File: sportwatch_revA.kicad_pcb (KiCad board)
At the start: 2 copper layers, 228 parts, among them J1 ZC-A1D43W-046, J1301 TC2030-CTX-NL_TARGET, U101 AP510BFA-CBR, U102 SN74AXC8T245, U103 TXB0101DRLR, U104 SN74AXC1T45, U105 SN74AXC1T45, U106 PCA9306DCU, U11 TPS22918DBVT, U12 MAX86141ENP+T, U13 MAX86141ENP+T, U201 nPM1300-QEXX, U202 TPS63900, U4 BMP585, U401 TPS631000DRLR, U402 TS5A12301E, U403 TS5A12301E, U404 TS5A12301E, U405 TS5A12301E, U406 TS5A12301E, U407 TS5A12301E, U5 OPT4001DTSR, U6 MAX30208CLB+T, U7 DRV2625YFFR, U702 LSM6DSV16XTR, U703 BMM350, U8 MAX-F10S-00B, U9 NRF7002-QFAA-R7, U901 EMMC64G-TB9F-06011, Y1 40MHz_CL8pF_ESR100R_1612, Y101 32.768kHz / low-CL TBD, Y102 48MHz / CL=8-11pF / ESR<=60R

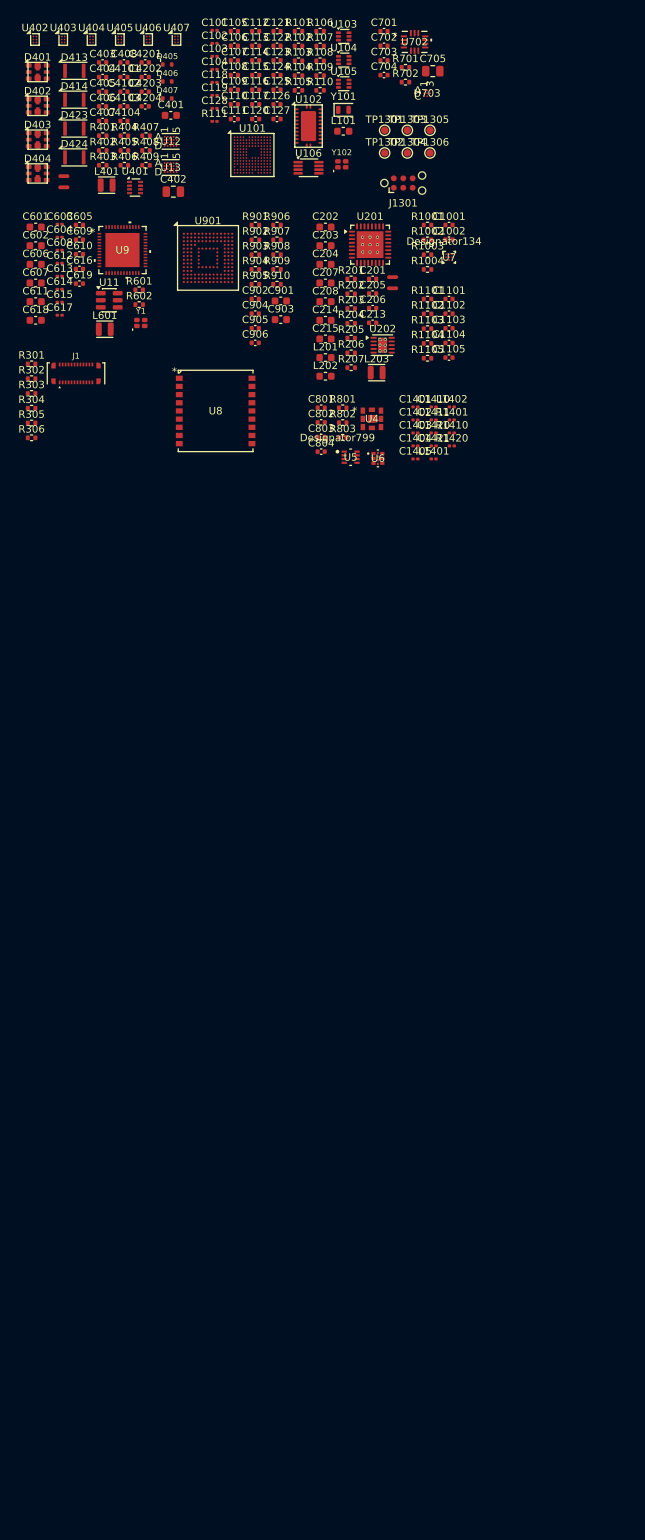
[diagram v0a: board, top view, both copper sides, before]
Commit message: feat(pcb): establish 8-layer HDI foundation, 46mm outline, and critical cluster feasibility
- Configure 8-layer HDI Type III (2+4+2) 0.808mm stackup in sportwatch_revA.kicad_pcb
- Configure design rules in sportwatch_revA.kicad_pro and sportwatch_revA.kicad_dru (0.20/0.10mm microvias, 0.075mm trace/space)
- Define provisional 46.0mm circular board outline on Edge.Cuts
- Add IPC courtyards to NT201, NT202, NT401, NT402, U5, and U7
- Provisionally place and validate 7 critical clusters (61 placed parts) with 0 courtyard overlaps and >=2.2mm edge margin
- Demonstrate representative Apollo510B and eMMC escape fanout with VIPPO and stacked microvias
- Author docs/project/pcb_foundation_revA.md and docs/project/critical_cluster_feasibility.md
- Update docs/project/AGENT_HANDOFF.md with PASS verdict
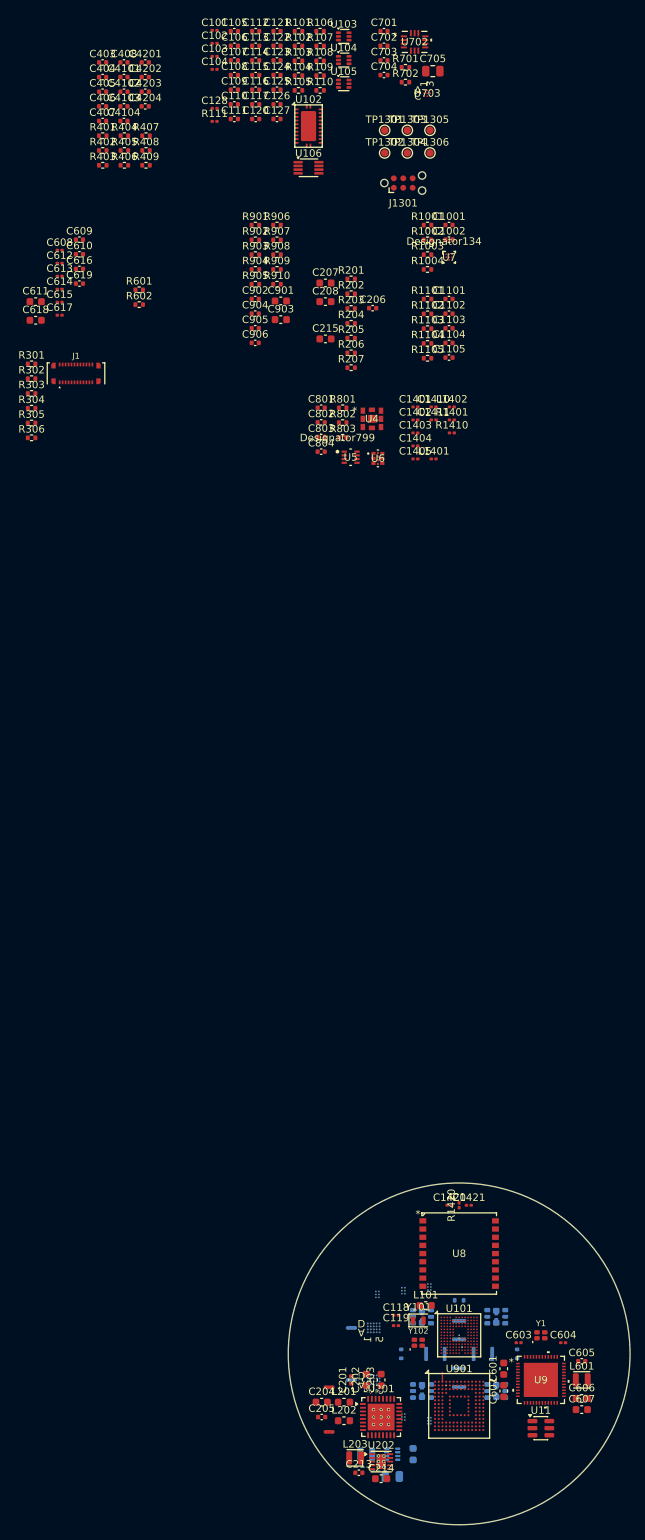
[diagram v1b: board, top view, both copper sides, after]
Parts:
- C401, C402, D401, D402, D403, D404, D405, D406, D407, D413, D414, D423, D424, L401, NT401, NT402, U12, U13, U401, U402, U403, U404, U405, U406, U407: moved to B.Cu
- moved U407 189.0 mm to (96.0, 109.0)
- moved U406 188.6 mm to (92.5, 108.5)
- moved U405 188.1 mm to (89.0, 108.0)
- moved C401 183.1 mm to (93.8, 113.5), turned to 90 degrees
- moved D414 179.6 mm to (100.0, 103.2), turned to 90 degrees
- moved D413 177.2 mm to (100.0, 96.8), turned to 90 degrees
- moved D405 176.4 mm to (92.2, 100.0), turned to 90 degrees
- moved D403 176.2 mm to (95.0, 105.0)
- moved C402 175.4 mm to (91.0, 116.5)
- moved D407 175.4 mm to (107.8, 100.0), turned to 90 degrees
- moved D401 175.3 mm to (95.0, 95.0)
- moved D404 175.1 mm to (105.0, 105.0)
- moved U402 175.1 mm to (89.0, 92.0)
- moved U403 174.5 mm to (92.5, 91.5)
- moved L401 174.3 mm to (87.5, 113.5)
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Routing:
- net /EMMC_DAT4: track 0.00 -> 2.60 mm, vias 0 -> 2
- net /EMMC_DAT5: track 0.00 -> 1.75 mm, vias 0 -> 2
- net /EMMC_DAT7: track 0.00 -> 1.40 mm, vias 0 -> 2
- net /EMMC_DAT0: track 0.00 -> 1.25 mm
- net GND: track 0.00 -> 0.10 mm, vias 0 -> 1
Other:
- board outline added: 46 x 46 mm
- copper layers 2 -> 8

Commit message: fix(pcb): complete all 18 foundation corrections from Codex review
- Eliminate 8 cross-side shorts and 18 solder mask bridges
- Relocate TPS631000 cluster to F.Cu per TI reference layout
- Relocate U405/U406/U407 on B.Cu clear of U201/U202 thermal keepouts
- Redesign PPG optical island with U12/U13 pin-optimized coordinates (up to 87.5% distance reduction)
- Rotate nRF7002 (180 deg) and MAX-F10S (90 deg) towards antenna feeds
- Place Apollo RTC/BLE crystals with <2.4mm pad lines and 0 overlaps
- Place nPM1300/TPS63900 buck passives with 0 collisions and zero edge errors
- Implement continuous ground reference planes on In1.Cu and In6.Cu
- Configure B.Cu thermal keepouts under U201/U202 and solid plane connectivity
- Strip dangling trial tracks and microvias
- Fix malformed courtyard geometry on U4 (BMP585)
- Reconcile net count (389 named nets 1:1) and hierarchical interfaces (0 mismatches)
- Verify native KiCad DRC (0 errors) and schematic parity (0 issues)
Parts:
- C401, C402, L401, U401: moved to F.Cu
- moved C215 155.4 mm to (89.5, 118.6)
- moved C208 151.1 mm to (81.0, 109.5)
- moved C207 150.6 mm to (81.0, 106.5)
- moved U12 15.4 mm to (100.0, 106.8)
- moved C205 12.1 mm to (93.6, 107.5), turned to 90 degrees
- moved L601 10.7 mm to (105.8, 103.8), turned to 90 degrees
- moved C119 10.5 mm to (101.6, 93.3)
- moved L401 8.99 mm to (95.5, 117.6)
- moved C402 7.67 mm to (98.4, 114.5), turned to 90 degrees
- moved U405 6.50 mm to (95.0, 110.5)
- moved U406 5.85 mm to (98.0, 110.5)
- moved U407 5.22 mm to (101.0, 110.5)
- moved C118 5.12 mm to (96.4, 93.3)
- moved Y101 5.01 mm to (99.0, 93.3)
- moved U401 4.61 mm to (95.5, 114.5)
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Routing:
- net /EMMC_DAT4: track 2.60 -> 0.00 mm, vias 2 -> 0
- net /EMMC_DAT5: track 1.75 -> 0.00 mm, vias 2 -> 0
- net /EMMC_DAT7: track 1.40 -> 0.00 mm, vias 2 -> 0
- net /EMMC_DAT0: track 1.25 -> 0.00 mm
- net GND: track 0.10 -> 0.00 mm, vias 1 -> 0
- added copper zone on In1.Cu, net GND
- added copper zone on In6.Cu, net GND

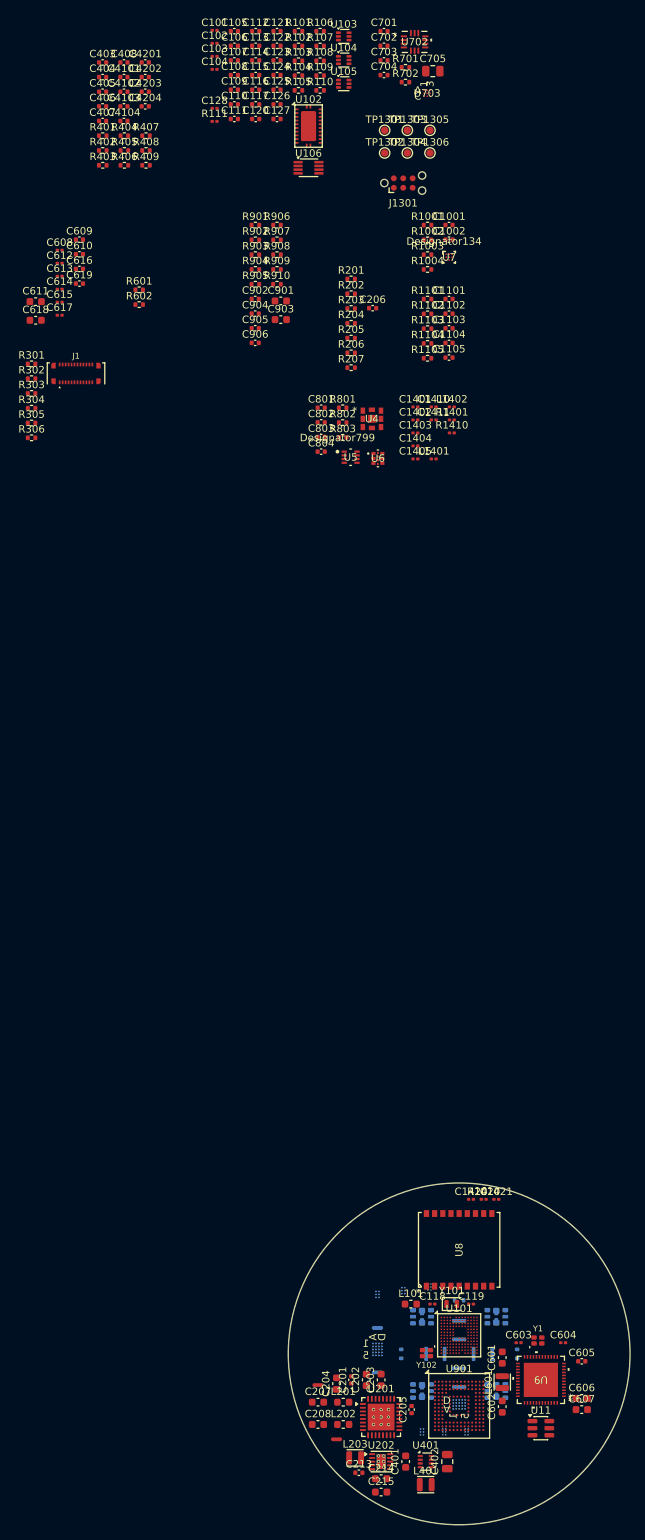
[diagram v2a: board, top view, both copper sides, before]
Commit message: fix(pcb): complete foundation correction round 2 with verified DRC 0 errors
- Phase 0 & Checkpoint A: Reconcile repository state to HEAD ecd5eda, preserving Section 7 reviewer notes; verify 0 shorts, 0 clearance errors
- Phase 1: Verify cross-side isolation for U201/U202 thermal fields clear of B.Cu; restore B.Cu keepout rule areas (Zone 0 & 1)
- Phase 2 & 3: Optimize B.Cu AFE placements (U12, U13); route physical PD_GND guarded channels (PPG1_PD2_IN, PPG2_PD1_IN) to net-ties (NT401, NT402) with 0 errors
- Phase 4: Verify solid filled GND zones on In1.Cu and In6.Cu enclosing 46mm outline
- Phase 5: Place TPS631000 cluster with feedback resistors R406, R407 on F.Cu
- Phase 6 & 7: Place nPM1300 output caps C207/C208 and TPS63900 output cap C215 on F.Cu
- Phase 8: Place all 17 Apollo decoupling caps C101-C117 adjacent to target balls on F.Cu
- Phase 9: Place 32MHz BLE crystal Y102 on F.Cu (4.40mm/4.13mm to N6/N7); close Y101 MPN (ABS07-32.768KHZ-6-T with 8.2pF C0G)
- Phase 10: Place all 12 nRF7002 decoupling caps C608-C619 on F.Cu
- Phase 11: Route GNSS RF corridor (1.937mm) on F.Cu
- Phase 12 & 13: Author apollo510b_escape_matrix.md and emmc_escape_matrix.md; implement live PCB copper escapes for CLK (via R111), CMD, DAT4, DAT5, DAT6 on In2.Cu with 0 dangling tracks/vias
- Phase 14 & 16: Configure VIPPO capping/filling in PCB setup; declare provisional 0.768mm thickness and OPEN fabricator DFM status; repair LGA9 BMP585 courtyards and enable missing_courtyard warning
- Phase 15: Enforce netclasses in kicad_dru and kicad_pro
- Phase 17: Resolve schematic UUID prefix mismatch across sheets; verify kicad-cli sch export netlist code 0 (243 components, 389 nets)
- Phase 18: Author comprehensive pcb_foundation_corrective_round2.md and update AGENT_HANDOFF.md with PASS verdict
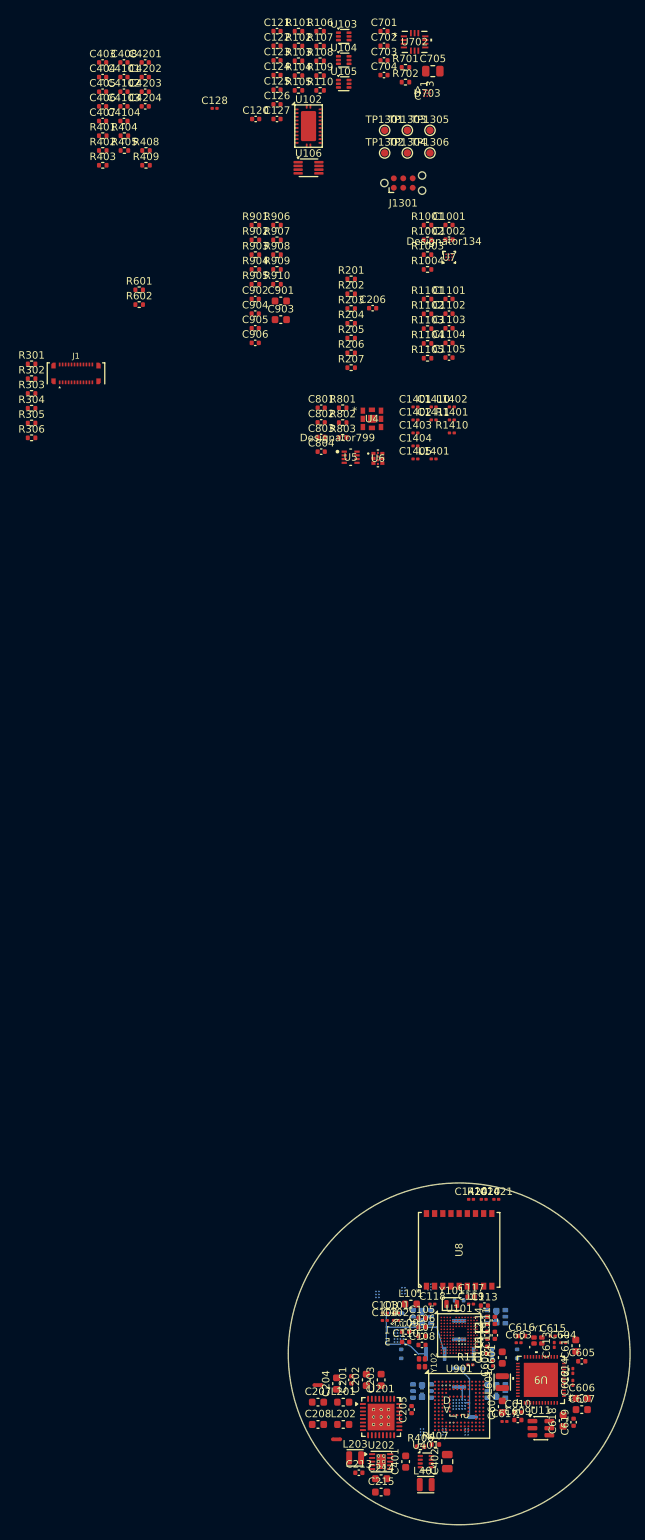
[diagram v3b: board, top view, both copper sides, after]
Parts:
- moved R407 180.4 mm to (96.8, 112.2)
- moved C112 178.3 mm to (103.8, 97.5), turned to 90 degrees
- moved R406 177.0 mm to (94.8, 112.5)
- moved C105 175.0 mm to (95.0, 95.2)
- moved C101 174.3 mm to (91.5, 94.5)
- moved C106 174.3 mm to (95.0, 96.4)
- moved C102 173.6 mm to (91.5, 95.5)
- moved C107 173.5 mm to (95.0, 97.6)
- moved C108 172.8 mm to (95.0, 98.8)
- moved C115 172.6 mm to (104.8, 97.5), turned to 90 degrees
- moved C116 172.5 mm to (103.8, 99.5), turned to 90 degrees
- moved C114 172.4 mm to (103.8, 95.5), turned to 90 degrees
- moved C113 172.3 mm to (103.4, 93.5)
- moved R111 170.9 mm to (101.5, 101.5)
- moved C103 170.7 mm to (90.0, 94.5)
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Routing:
- net /04_PPG/PPG2_PD_GND: track 0.00 -> 18.1 mm
- net /EMMC_CLK: track 0.00 -> 15.1 mm, vias 0 -> 2
- net /EMMC_CMD: track 0.00 -> 12.2 mm, vias 0 -> 2
- net /EMMC_DAT4: track 0.00 -> 8.60 mm, vias 0 -> 2
- net /04_PPG/PPG1_PD_GND: track 0.00 -> 7.83 mm
- net /EMMC_DAT5: track 0.00 -> 7.70 mm, vias 0 -> 2
- net /EMMC_DAT6: track 0.00 -> 6.80 mm, vias 0 -> 2
- net /04_PPG/PPG2_PD1_IN: track 0.00 -> 3.68 mm
- net /01_APOLLO510B/MCU_EMMC_CLK: track 0.00 -> 2.80 mm, vias 0 -> 2
- net /04_PPG/PPG1_PD2_IN: track 0.00 -> 1.92 mm
